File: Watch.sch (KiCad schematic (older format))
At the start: 1 part

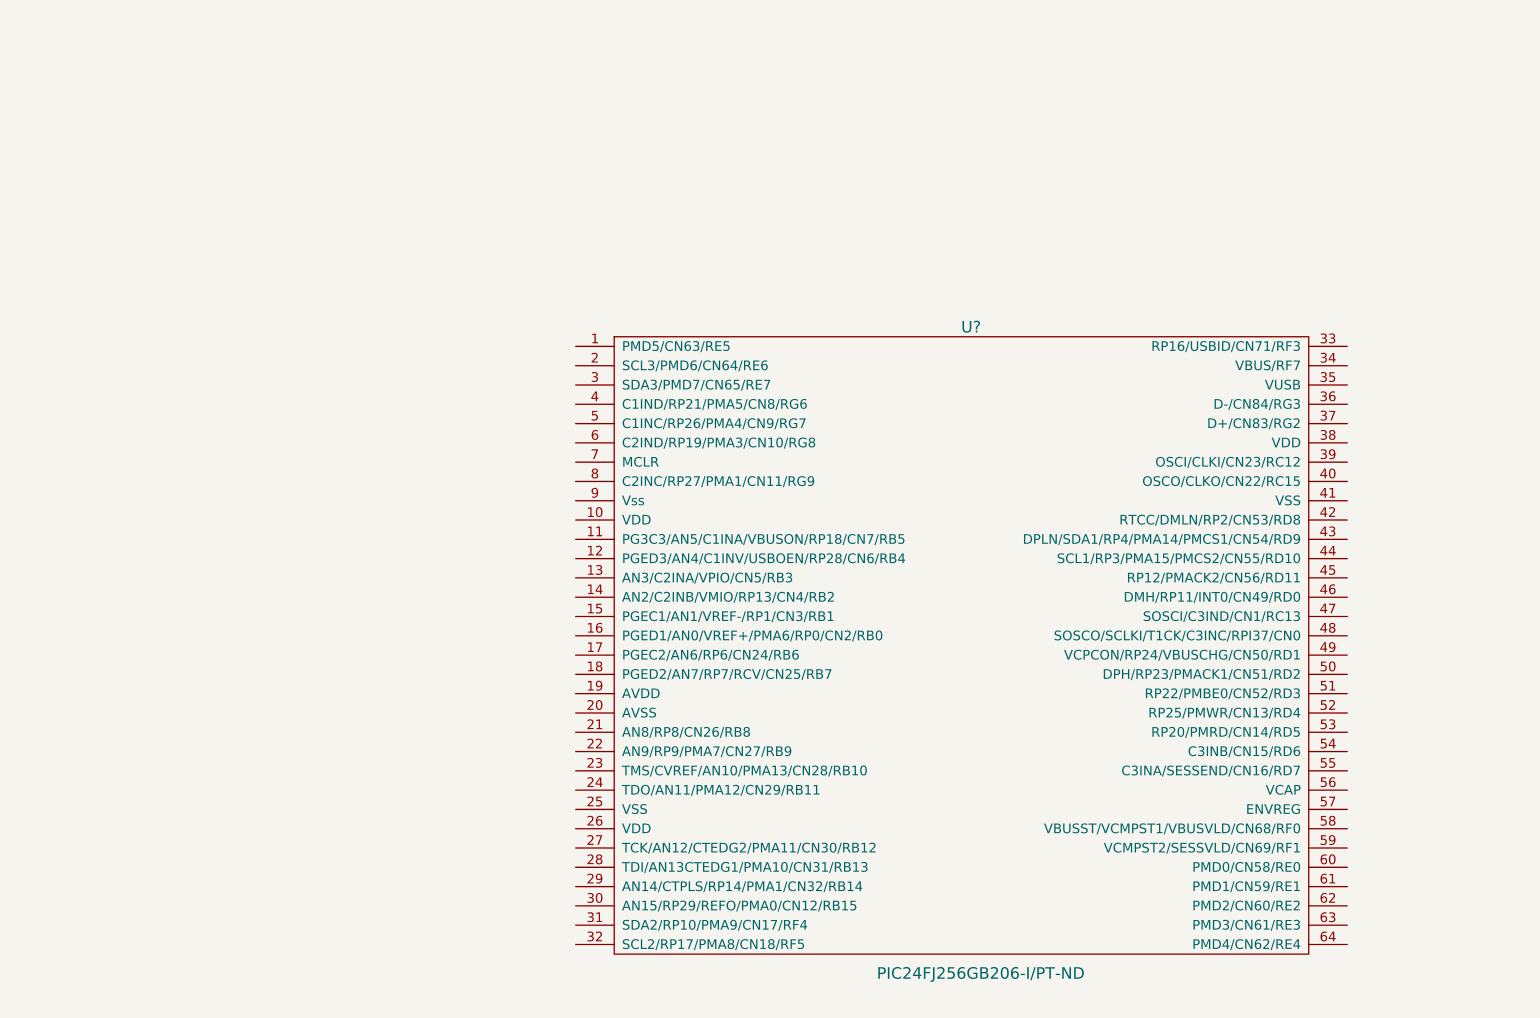
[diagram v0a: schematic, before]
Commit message: added decoupling caps for MCU
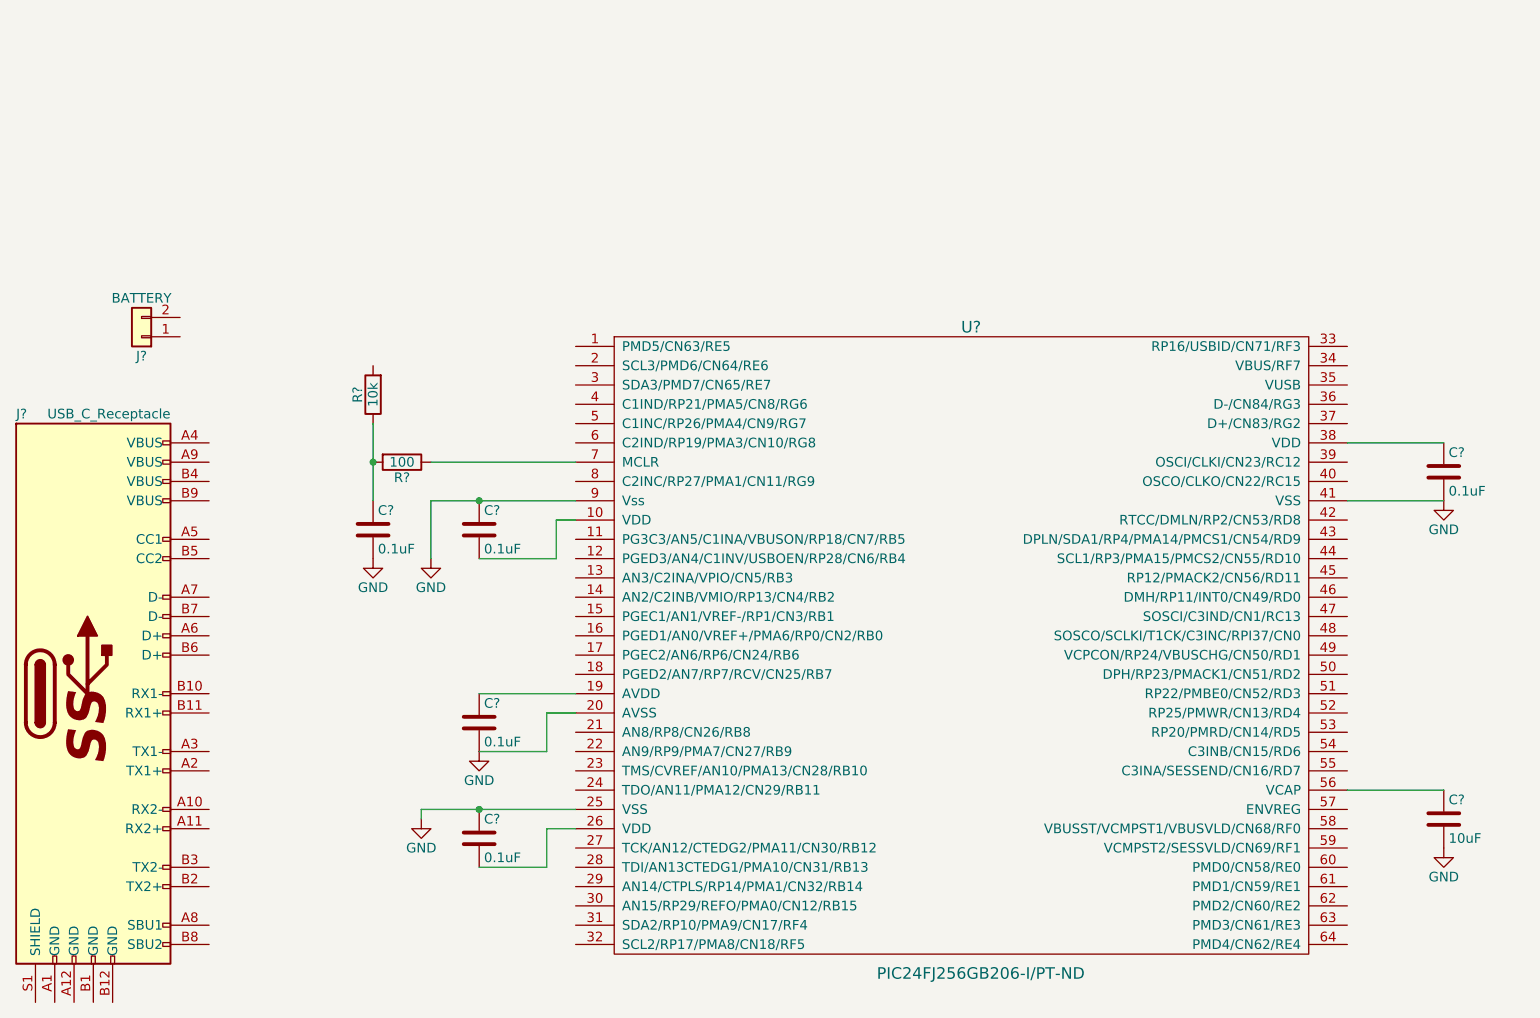
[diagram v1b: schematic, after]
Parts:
- added C? (x5): 0.1uF, symbol C
- added C?: 10uF, symbol C
- added J?: BATTERY, symbol Conn_01x02
- added J?: USB_C_Receptacle, symbol USB_C_Receptacle
- added R?: 100, symbol R
- added R?: 10k, symbol R
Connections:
- net at U?.10 (VDD): now also C?.2
- net at U?.19 (AVDD): now also C?.1
- net GND: now reaches U?.20 (AVSS)
- net GND: now also U?.25 (VSS), U?.41 (VSS), U?.9 (Vss), C?.1, C?.1, C?.2, C?.2, C?.2, C?.2
- net at U?.26 (VDD): now also C?.2
- net at U?.38 (VDD): now also C?.1
- net at U?.56 (VCAP): now also C?.1
- net at U?.7 (MCLR): now also R?.1
- new net: C?.1, R?.1, R?.2
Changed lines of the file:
@@
 	1    0    0    -1
 $EndComp
+$Comp
+L Conn_01x02 J?
+U 1 1 5B74C839
+P 1350 2900
+F 0 "J?" H 1350 3000 50  0000 C CNN
+F 1 "BATTERY" H 1350 2700 50  0000 C CNN
+F 2 "" H 1350 2900 50  0001 C CNN
+F 3 "" H 1350 2900 50  0001 C CNN
+	1    1350 2900
+	-1   0    0    1
+$EndComp
+$Comp
+L USB_C_Receptacle J?
+U 1 1 5B74C8F5
+P 1100 4750
+F 0 "J?" H 700 6200 50  0000 L CNN
+F 1 "USB_C_Receptacle" H 1500 6200 50  0000 R CNN
+F 2 "" H 1250 4750 50  0001 C CNN
+F 3 "" H 1250 4750 50  0001 C CNN
+	1    1100 4750
+	1    0    0    -1
+$EndComp
+$Comp
+L R R?
+U 1 1 5B74FA50
+P 2700 3550
+F 0 "R?" V 2780 3550 50  0000 C CNN
+F 1 "100" V 2700 3550 50  0000 C CNN
+F 2 "" V 2630 3550 50  0001 C CNN
+F 3 "" H 2700 3550 50  0001 C CNN
+	1    2700 3550
+	0    1    1    0
+$EndComp
+$Comp
+L R R?
+U 1 1 5B74FB1A
+P 2550 3200
+F 0 "R?" V 2630 3200 50  0000 C CNN
+F 1 "10k" V 2550 3200 50  0000 C CNN
+F 2 "" V 2480 3200 50  0001 C CNN
+F 3 "" H 2550 3200 50  0001 C CNN
+	1    2550 3200
+	-1   0    0    1
+$EndComp
+$Comp
+L C C?
+U 1 1 5B74FB4E
+P 2550 3900
+F 0 "C?" H 2575 4000 50  0000 L CNN
+F 1 "0.1uF" H 2575 3800 50  0000 L CNN
+F 2 "" H 2588 3750 50  0001 C CNN
+F 3 "" H 2550 3900 50  0001 C CNN
+	1    2550 3900
+	1    0    0    -1
+$EndComp
+$Comp
+L GND #PWR?
+U 1 1 5B74FBB7
+P 2550 4050
+F 0 "#PWR?" H 2550 3800 50  0001 C CNN
+F 1 "GND" H 2550 3900 50  0000 C CNN
+F 2 "" H 2550 4050 50  0001 C CNN
+F 3 "" H 2550 4050 50  0001 C CNN
+	1    2550 4050
+	1    0    0    -1
+$EndComp
+Wire Wire Line
+	2850 3550 3600 3550
+Wire Wire Line
+	2550 3350 2550 3750
+Connection ~ 2550 3550
+$Comp
+L C C?
+U 1 1 5B74FD09
+P 3100 3900
+F 0 "C?" H 3125 4000 50  0000 L CNN
+F 1 "0.1uF" H 3125 3800 50  0000 L CNN
+F 2 "" H 3138 3750 50  0001 C CNN
+F 3 "" H 3100 3900 50  0001 C CNN
+	1    3100 3900
+	1    0    0    -1
+$EndComp
+Wire Wire Line
+	2850 3750 3600 3750
+Wire Wire Line
+	3100 4050 3500 4050
+Wire Wire Line
+	3500 4050 3500 3850
+Wire Wire Line
+	3500 3850 3600 3850
+$Comp
+L C C?
+U 1 1 5B74FECC
+P 3100 4900
+F 0 "C?" H 3125 5000 50  0000 L CNN
+F 1 "0.1uF" H 3125 4800 50  0000 L CNN
+F 2 "" H 3138 4750 50  0001 C CNN
+F 3 "" H 3100 4900 50  0001 C CNN
+	1    3100 4900
+	1    0    0    -1
+$EndComp
+Wire Wire Line
+	3600 4750 3100 4750
+Wire Wire Line
+	3100 5050 3450 5050
+Wire Wire Line
+	3450 5050 3450 4850
+Wire Wire Line
+	3450 4850 3600 4850
+$Comp
+L C C?
+U 1 1 5B74FF6E
+P 3100 5500
+F 0 "C?" H 3125 5600 50  0000 L CNN
+F 1 "0.1uF" H 3125 5400 50  0000 L CNN
+F 2 "" H 3138 5350 50  0001 C CNN
+F 3 "" H 3100 5500 50  0001 C CNN
+	1    3100 5500
+	1    0    0    -1
+$EndComp
+Wire Wire Line
+	2800 5350 3600 5350
+Wire Wire Line
+	3100 5650 3450 5650
+Wire Wire Line
+	3450 5650 3450 5450
+Wire Wire Line
+	3450 5450 3600 5450
+$Comp
+L C C?
+U 1 1 5B758727
+P 8100 3600
+F 0 "C?" H 8125 3700 50  0000 L CNN
+F 1 "0.1uF" H 8125 3500 50  0000 L CNN
+F 2 "" H 8138 3450 50  0001 C CNN
+F 3 "" H 8100 3600 50  0001 C CNN
+	1    8100 3600
+	1    0    0    -1
+$EndComp
+Wire Wire Line
+	7600 3450 8100 3450
+Wire Wire Line
+	8100 3750 7600 3750
+$Comp
+L C C?
+U 1 1 5B758A9B
+P 8100 5400
+F 0 "C?" H 8125 5500 50  0000 L CNN
+F 1 "10uF" H 8125 5300 50  0000 L CNN
+F 2 "" H 8138 5250 50  0001 C CNN
+F 3 "" H 8100 5400 50  0001 C CNN
+	1    8100 5400
+	1    0    0    -1
+$EndComp
+Wire Wire Line
+	7600 5250 8100 5250
+$Comp
+L GND #PWR?
+U 1 1 5B758BF3
+P 8100 5550
+F 0 "#PWR?" H 8100 5300 50  0001 C CNN
+F 1 "GND" H 8100 5400 50  0000 C CNN
+F 2 "" H 8100 5550 50  0001 C CNN
+F 3 "" H 8100 5550 50  0001 C CNN
+	1    8100 5550
+	1    0    0    -1
+$EndComp
+$Comp
+L GND #PWR?
+U 1 1 5B75A410
+P 8100 3750
+F 0 "#PWR?" H 8100 3500 50  0001 C CNN
+F 1 "GND" H 8100 3600 50  0000 C CNN
+F 2 "" H 8100 3750 50  0001 C CNN
+F 3 "" H 8100 3750 50  0001 C CNN
+	1    8100 3750
+	1    0    0    -1
+$EndComp
+$Comp
+L GND #PWR?
+U 1 1 5B75A43C
+P 3100 5050
+F 0 "#PWR?" H 3100 4800 50  0001 C CNN
+F 1 "GND" H 3100 4900 50  0000 C CNN
+F 2 "" H 3100 5050 50  0001 C CNN
+F 3 "" H 3100 5050 50  0001 C CNN
+	1    3100 5050
+	1    0    0    -1
+$EndComp
+$Comp
+L GND #PWR?
+U 1 1 5B75A570
+P 2800 5400
+F 0 "#PWR?" H 2800 5150 50  0001 C CNN
+F 1 "GND" H 2800 5250 50  0000 C CNN
+F 2 "" H 2800 5400 50  0001 C CNN
+F 3 "" H 2800 5400 50  0001 C CNN
+	1    2800 5400
+	1    0    0    -1
+$EndComp
+Wire Wire Line
+	2800 5400 2800 5350
+Connection ~ 3100 5350
+$Comp
+L GND #PWR?
+U 1 1 5B75A620
+P 2850 4050
+F 0 "#PWR?" H 2850 3800 50  0001 C CNN
+F 1 "GND" H 2850 3900 50  0000 C CNN
+F 2 "" H 2850 4050 50  0001 C CNN
+F 3 "" H 2850 4050 50  0001 C CNN
+	1    2850 4050
+	1    0    0    -1
+$EndComp
+Wire Wire Line
+	2850 4050 2850 3750
+Connection ~ 3100 3750
 $EndSCHEMATC

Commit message: added linear reg
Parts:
- added U?: LinearReg, symbol LinearReg
- U?: symbol PIC24FJ256GB206-I/PT-ND -> PIC24FJ256GB206-I/PT-ND-RESCUE-Watch
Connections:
- net GND: now also J?.1 (Pin_1)
- net 3v: now reaches C?.2, U?.10 (VDD)
- net 3v: now also C?.1, C?.1, C?.1, C?.2, R?.2, U?.19 (AVDD), U?.26 (VDD), U?.38 (VDD), U?.56 (VCAP), U?.2 (Output)
- net 3.7v: now reaches J?.2 (Pin_2)
- net 3.7v: now also U?.1 (Input)
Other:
- moved on the sheet: C?, J?, R?
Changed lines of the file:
@@
 EESchema Schematic File Version 2
+LIBS:Watch-rescue
 LIBS:power
 LIBS:device
@@
 LIBS:valves
 LIBS:PIC
+LIBS:Placeholders
 LIBS:Watch-cache
 EELAYER 25 0
@@
 $EndDescr
 $Comp
-L PIC24FJ256GB206-I/PT-ND U?
+L PIC24FJ256GB206-I/PT-ND-RESCUE-Watch U?
 U 1 1 5B74C7A7
 P 4500 3350
@@
 L Conn_01x02 J?
 U 1 1 5B74C839
-P 1350 2900
-F 0 "J?" H 1350 3000 50  0000 C CNN
-F 1 "BATTERY" H 1350 2700 50  0000 C CNN
-F 2 "" H 1350 2900 50  0001 C CNN
-F 3 "" H 1350 2900 50  0001 C CNN
-	1    1350 2900
+P 1350 2200
+F 0 "J?" H 1350 2300 50  0000 C CNN
+F 1 "BATTERY" H 1350 2000 50  0000 C CNN
+F 2 "" H 1350 2200 50  0001 C CNN
+F 3 "" H 1350 2200 50  0001 C CNN
+	1    1350 2200
 	-1   0    0    1
 $EndComp
@@
 L R R?
 U 1 1 5B74FA50
-P 2700 3550
-F 0 "R?" V 2780 3550 50  0000 C CNN
-F 1 "100" V 2700 3550 50  0000 C CNN
-F 2 "" V 2630 3550 50  0001 C CNN
-F 3 "" H 2700 3550 50  0001 C CNN
-	1    2700 3550
+P 2600 3550
+F 0 "R?" V 2680 3550 50  0000 C CNN
+F 1 "100" V 2600 3550 50  0000 C CNN
+F 2 "" V 2530 3550 50  0001 C CNN
+F 3 "" H 2600 3550 50  0001 C CNN
+	1    2600 3550
 	0    1    1    0
 $EndComp
@@
 L R R?
 U 1 1 5B74FB1A
-P 2550 3200
-F 0 "R?" V 2630 3200 50  0000 C CNN
-F 1 "10k" V 2550 3200 50  0000 C CNN
-F 2 "" V 2480 3200 50  0001 C CNN
-F 3 "" H 2550 3200 50  0001 C CNN
-	1    2550 3200
+P 2450 3200
+F 0 "R?" V 2530 3200 50  0000 C CNN
+F 1 "10k" V 2450 3200 50  0000 C CNN
+F 2 "" V 2380 3200 50  0001 C CNN
+F 3 "" H 2450 3200 50  0001 C CNN
+	1    2450 3200
 	-1   0    0    1
 $EndComp
@@
 L C C?
 U 1 1 5B74FB4E
-P 2550 3900
-F 0 "C?" H 2575 4000 50  0000 L CNN
-F 1 "0.1uF" H 2575 3800 50  0000 L CNN
-F 2 "" H 2588 3750 50  0001 C CNN
-F 3 "" H 2550 3900 50  0001 C CNN
-	1    2550 3900
+P 2450 3900
+F 0 "C?" H 2475 4000 50  0000 L CNN
+F 1 "0.1uF" H 2475 3800 50  0000 L CNN
+F 2 "" H 2488 3750 50  0001 C CNN
+F 3 "" H 2450 3900 50  0001 C CNN
+	1    2450 3900
 	1    0    0    -1
 $EndComp
@@
 L GND #PWR?
 U 1 1 5B74FBB7
-P 2550 4050
-F 0 "#PWR?" H 2550 3800 50  0001 C CNN
-F 1 "GND" H 2550 3900 50  0000 C CNN
-F 2 "" H 2550 4050 50  0001 C CNN
-F 3 "" H 2550 4050 50  0001 C CNN
-	1    2550 4050
-	1    0    0    -1
-$EndComp
-Wire Wire Line
-	2850 3550 3600 3550
-Wire Wire Line
-	2550 3350 2550 3750
-Connection ~ 2550 3550
+P 2450 4050
+F 0 "#PWR?" H 2450 3800 50  0001 C CNN
+F 1 "GND" H 2450 3900 50  0000 C CNN
+F 2 "" H 2450 4050 50  0001 C CNN
+F 3 "" H 2450 4050 50  0001 C CNN
+	1    2450 4050
+	1    0    0    -1
+$EndComp
+Wire Wire Line
+	2750 3550 3600 3550
+Wire Wire Line
+	2450 3350 2450 3750
+Connection ~ 2450 3550
 $Comp
 L C C?
@@
 $EndComp
 Wire Wire Line
-	2850 3750 3600 3750
-Wire Wire Line
-	3100 4050 3500 4050
+	2750 3750 3600 3750
+Wire Wire Line
+	3000 4050 3500 4050
 Wire Wire Line
 	3500 4050 3500 3850
@@
 $EndComp
 Wire Wire Line
-	3600 4750 3100 4750
+	3000 4750 3600 4750
 Wire Wire Line
 	3100 5050 3450 5050
@@
 $EndComp
 Wire Wire Line
-	2800 5350 3600 5350
-Wire Wire Line
-	3100 5650 3450 5650
+	2650 5350 3600 5350
+Wire Wire Line
+	3000 5650 3450 5650
 Wire Wire Line
 	3450 5650 3450 5450
@@
 $EndComp
 Wire Wire Line
-	7600 3450 8100 3450
+	7600 3450 8250 3450
 Wire Wire Line
 	8100 3750 7600 3750
@@
 $EndComp
 Wire Wire Line
-	7600 5250 8100 5250
+	7600 5250 8250 5250
 $Comp
 L GND #PWR?
@@
 L GND #PWR?
 U 1 1 5B75A570
-P 2800 5400
-F 0 "#PWR?" H 2800 5150 50  0001 C CNN
-F 1 "GND" H 2800 5250 50  0000 C CNN
-F 2 "" H 2800 5400 50  0001 C CNN
-F 3 "" H 2800 5400 50  0001 C CNN
-	1    2800 5400
-	1    0    0    -1
-$EndComp
-Wire Wire Line
-	2800 5400 2800 5350
+P 2650 5600
+F 0 "#PWR?" H 2650 5350 50  0001 C CNN
+F 1 "GND" H 2650 5450 50  0000 C CNN
+F 2 "" H 2650 5600 50  0001 C CNN
+F 3 "" H 2650 5600 50  0001 C CNN
+	1    2650 5600
+	1    0    0    -1
+$EndComp
+Wire Wire Line
+	2650 5600 2650 5350
 Connection ~ 3100 5350
 $Comp
 L GND #PWR?
 U 1 1 5B75A620
-P 2850 4050
-F 0 "#PWR?" H 2850 3800 50  0001 C CNN
-F 1 "GND" H 2850 3900 50  0000 C CNN
-F 2 "" H 2850 4050 50  0001 C CNN
-F 3 "" H 2850 4050 50  0001 C CNN
-	1    2850 4050
-	1    0    0    -1
-$EndComp
-Wire Wire Line
-	2850 4050 2850 3750
+P 2750 4050
+F 0 "#PWR?" H 2750 3800 50  0001 C CNN
+F 1 "GND" H 2750 3900 50  0000 C CNN
+F 2 "" H 2750 4050 50  0001 C CNN
+F 3 "" H 2750 4050 50  0001 C CNN
+	1    2750 4050
+	1    0    0    -1
+$EndComp
+Wire Wire Line
+	2750 4050 2750 3750
 Connection ~ 3100 3750
+$Comp
+L LinearReg U?
+U 1 1 5B75AE22
+P 3850 1950
+F 0 "U?" H 3850 1900 60  0000 C CNN
+F 1 "LinearReg" H 3850 1550 60  0000 C CNN
+F 2 "" H 3850 1950 60  0001 C CNN
+F 3 "" H 3850 1950 60  0001 C CNN
+	1    3850 1950
+	1    0    0    -1
+$EndComp
+$Comp
+L GND #PWR?
+U 1 1 5B75AF29
+P 1550 2200
+F 0 "#PWR?" H 1550 1950 50  0001 C CNN
+F 1 "GND" H 1550 2050 50  0000 C CNN
+F 2 "" H 1550 2200 50  0001 C CNN
+F 3 "" H 1550 2200 50  0001 C CNN
+	1    1550 2200
+	1    0    0    -1
+$EndComp
+Text GLabel 1550 2100 2    60   Input ~ 0
+3.7v
+Text GLabel 3250 2150 0    60   Input ~ 0
+3.7v
+Text GLabel 4400 2150 2    60   Input ~ 0
+3v
+Text GLabel 2450 3050 1    60   Input ~ 0
+3v
+Text GLabel 3000 4050 0    60   Input ~ 0
+3v
+Connection ~ 3100 4050
+Text GLabel 3000 4750 0    60   Input ~ 0
+3v
+Text GLabel 3000 5650 0    60   Input ~ 0
+3v
+Connection ~ 3100 4750
+Connection ~ 3100 5650
+Text GLabel 8250 3450 2    60   Input ~ 0
+3v
+Text GLabel 8250 5250 2    60   Input ~ 0
+3v
+Connection ~ 8100 5250
+Connection ~ 8100 3450
 $EndSCHEMATC

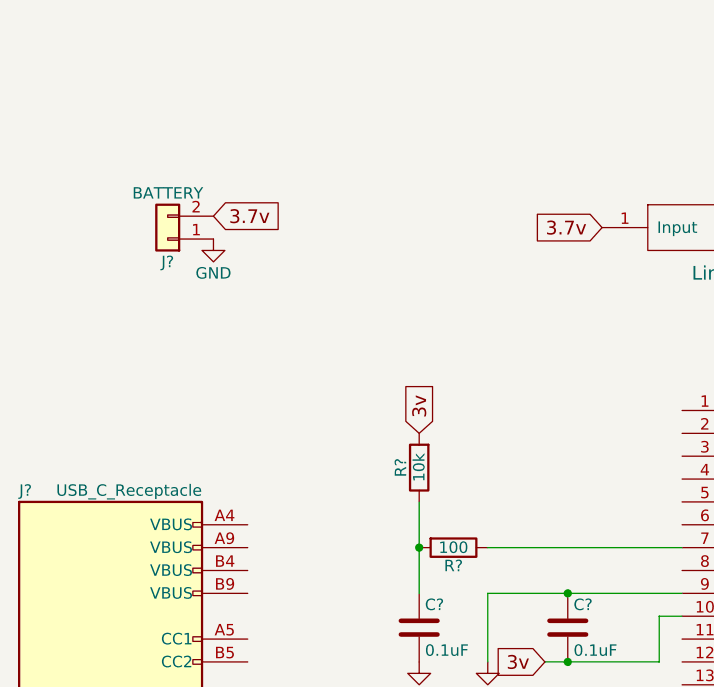
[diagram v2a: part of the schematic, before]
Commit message: Added charging circuitry
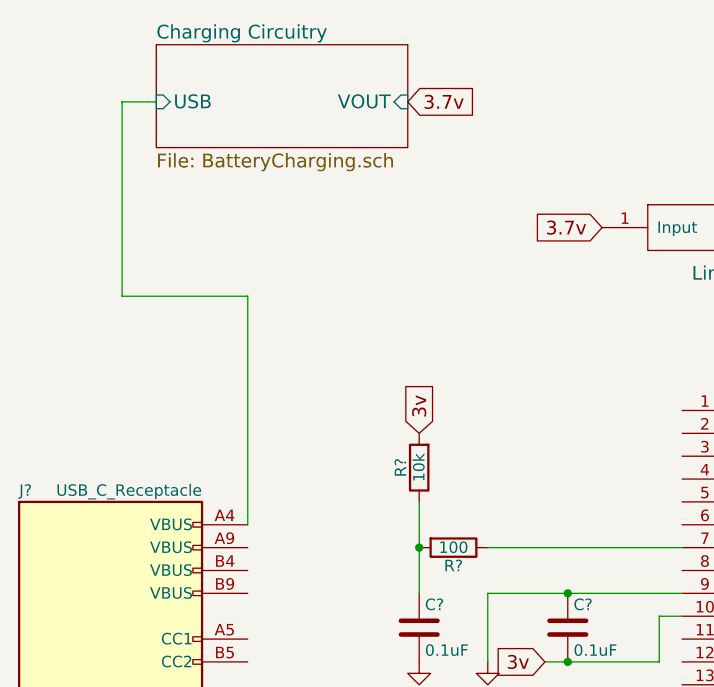
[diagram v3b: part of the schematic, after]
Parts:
- removed J?: BATTERY, symbol Conn_01x02
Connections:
- net Charging Circuitry/USB: now reaches J?.A4 (VBUS)
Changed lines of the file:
@@
 LIBS:PIC
 LIBS:Placeholders
+LIBS:Watch Parts
 LIBS:Watch-cache
 EELAYER 25 0
@@
 $Descr A4 11693 8268
 encoding utf-8
-Sheet 1 1
+Sheet 1 2
 Title ""
 Date ""
@@
 $EndComp
 $Comp
-L Conn_01x02 J?
-U 1 1 5B74C839
-P 1350 2200
-F 0 "J?" H 1350 2300 50  0000 C CNN
-F 1 "BATTERY" H 1350 2000 50  0000 C CNN
-F 2 "" H 1350 2200 50  0001 C CNN
-F 3 "" H 1350 2200 50  0001 C CNN
-	1    1350 2200
-	-1   0    0    1
-$EndComp
-$Comp
 L USB_C_Receptacle J?
 U 1 1 5B74C8F5
@@
 	1    0    0    -1
 $EndComp
-$Comp
-L GND #PWR?
-U 1 1 5B75AF29
-P 1550 2200
-F 0 "#PWR?" H 1550 1950 50  0001 C CNN
-F 1 "GND" H 1550 2050 50  0000 C CNN
-F 2 "" H 1550 2200 50  0001 C CNN
-F 3 "" H 1550 2200 50  0001 C CNN
-	1    1550 2200
-	1    0    0    -1
-$EndComp
-Text GLabel 1550 2100 2    60   Input ~ 0
-3.7v
 Text GLabel 3250 2150 0    60   Input ~ 0
 3.7v
@@
 Connection ~ 8100 5250
 Connection ~ 8100 3450
+$Sheet
+S 1300 1350 1100 450
+U 5B80199A
+F0 "Charging Circuitry" 60
+F1 "BatteryCharging.sch" 60
+F2 "VOUT" I R 2400 1600 60
+F3 "USB" I L 1300 1600 60
+$EndSheet
+Wire Wire Line
+	1700 3450 1700 2450
+Wire Wire Line
+	1700 2450 1150 2450
+Wire Wire Line
+	1150 2450 1150 1600
+Wire Wire Line
+	1150 1600 1300 1600
+Text GLabel 2400 1600 2    60   Input ~ 0
+3.7v
 $EndSCHEMATC
